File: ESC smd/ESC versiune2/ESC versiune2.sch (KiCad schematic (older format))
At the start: 92 parts, among them J1 Conn_01x03, J2 Conn_01x03, J3 Conn_01x03, J4 Conn_01x03, J5 Conn_01x02, J6 Conn_01x03, J7 Conn_01x02, Q3 IRLB8721PBF, Q4 IRLB8721PBF, Q5 IRLB8721PBF, Q6 IRLB8721PBF, Q7 IRLB8721PBF, Q8 IRLB8721PBF, U1 L7805, U2 ACS711xLCTR-12AB, U3 LP2950-3.3_TO92, U4 IR2101, U5 IR2101, U6 IR2101, U7 LM393, U8 LM393

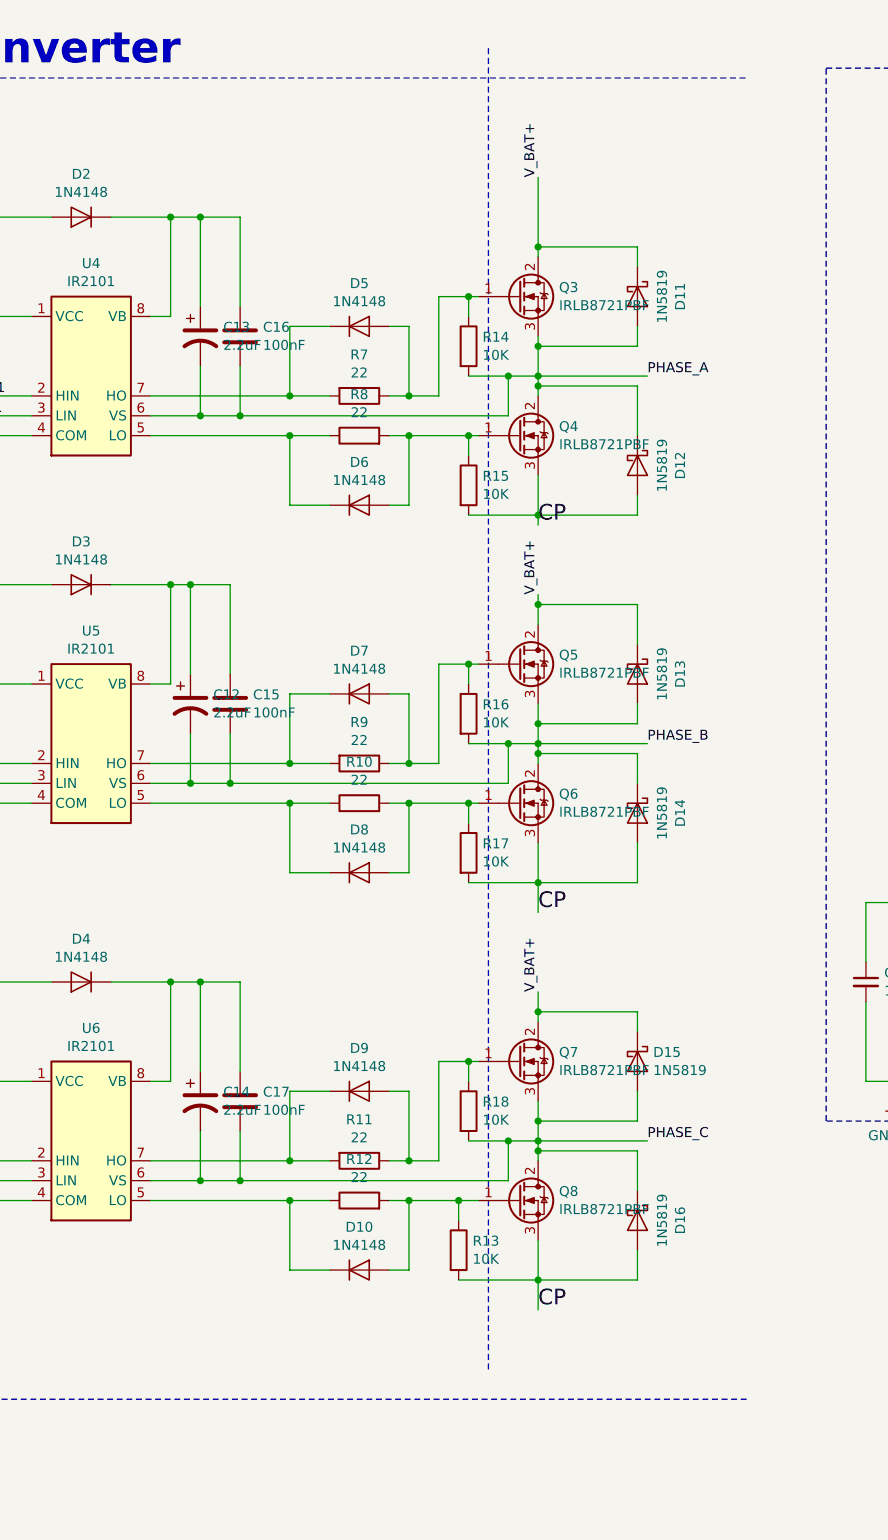
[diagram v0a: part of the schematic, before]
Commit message: SMD version
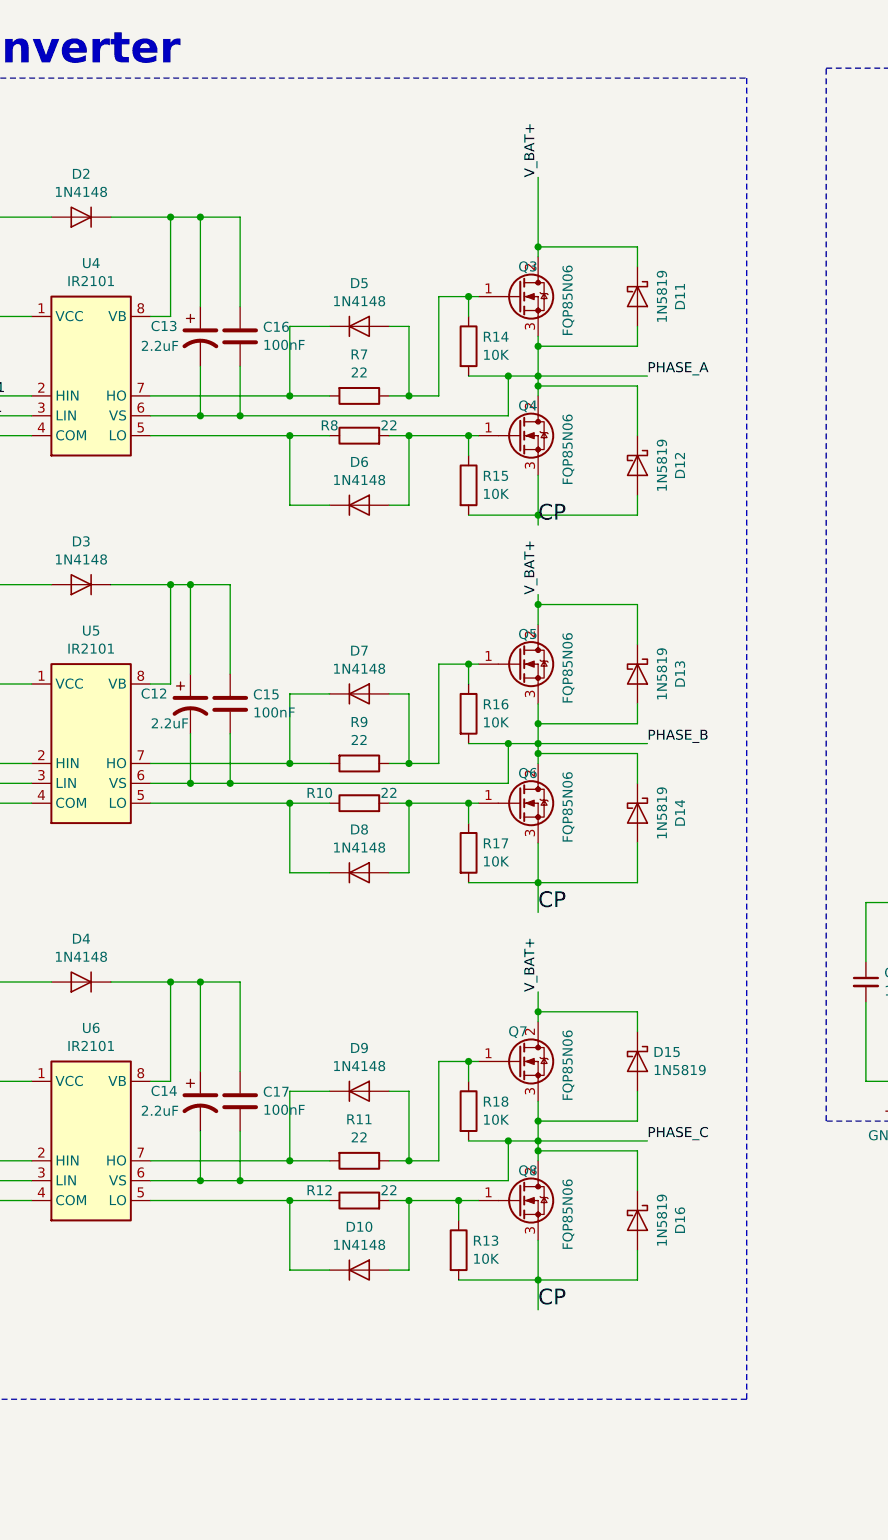
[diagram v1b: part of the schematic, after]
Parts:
- Q3, Q4, Q5, Q6, Q7, Q8: value IRLB8721PBF -> FQP85N06
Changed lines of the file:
@@
 Wire Wire Line
 	8000 4300 8200 4300
-Connection ~ 8000 4300
 Wire Wire Line
 	8000 4750 8000 4300
@@
 	10800 8400 5400 8400
 Wire Notes Line
-	9500 1600 9500 8250
+	10800 1750 10800 8400
 Wire Notes Line
 	5400 1750 10800 1750
@@
 AR Path="/5CB0A3AA" Ref="R12"  Part="1"
 AR Path="/5CB00088/5CB0A3AA" Ref="R?"  Part="1"
-F 0 "R12" V 9057 7400 50  0000 C CNN
-F 1 "22" V 8966 7400 50  0000 C CNN
+F 0 "R12" V 8900 7600 50  0000 C CNN
+F 1 "22" V 8900 7250 50  0000 C CNN
 F 2 "Resistor_SMD:R_2512_6332Metric_Pad1.52x3.35mm_HandSolder" V 8780 7400 50  0001 C CNN
 F 3 "~" H 8850 7400 50  0001 C CNN
@@
 	8200 4300 8200 4750
 Wire Wire Line
-	8000 5300 8200 5300
-Wire Wire Line
-	8200 5300 9600 5300
-Connection ~ 8200 5300
-Wire Wire Line
 	8200 5050 8200 5300
 $Comp
@@
 AR Path="/5CB0A348" Ref="R10"  Part="1"
 AR Path="/5CB00088/5CB0A348" Ref="R?"  Part="1"
-F 0 "R10" V 9057 5400 50  0000 C CNN
-F 1 "22" V 8966 5400 50  0000 C CNN
+F 0 "R10" V 8900 5600 50  0000 C CNN
+F 1 "22" V 8900 5250 50  0000 C CNN
 F 2 "Resistor_SMD:R_2512_6332Metric_Pad1.52x3.35mm_HandSolder" V 8780 5400 50  0001 C CNN
 F 3 "~" H 8850 5400 50  0001 C CNN
@@
 AR Path="/5CB0A2E7" Ref="R8"  Part="1"
 AR Path="/5CB00088/5CB0A2E7" Ref="R?"  Part="1"
-F 0 "R8" V 9057 3550 50  0000 C CNN
-F 1 "22" V 8966 3550 50  0000 C CNN
+F 0 "R8" V 8900 3700 50  0000 C CNN
+F 1 "22" V 8900 3400 50  0000 C CNN
 F 2 "Resistor_SMD:R_2512_6332Metric_Pad1.52x3.35mm_HandSolder" V 8780 3550 50  0001 C CNN
 F 3 "~" H 8850 3550 50  0001 C CNN
@@
 U 1 1 5CDD0D9C
 P 8050 3050
-F 0 "C13" H 8165 3096 50  0000 L CNN
-F 1 "2.2uF" H 8165 3005 50  0000 L CNN
+F 0 "C13" H 7800 3100 50  0000 L CNN
+F 1 "2.2uF" H 7750 3000 50  0000 L CNN
 F 2 "Capacitor_SMD:C_1206_3216Metric_Pad1.42x1.75mm_HandSolder" H 8050 3050 50  0001 C CNN
 F 3 "~" H 8050 3050 50  0001 C CNN
@@
 U 1 1 5CE448DD
 P 8000 4900
-F 0 "C12" H 8115 4946 50  0000 L CNN
-F 1 "2.2uF" H 8115 4855 50  0000 L CNN
+F 0 "C12" H 7750 4950 50  0000 L CNN
+F 1 "2.2uF" H 7800 4800 50  0000 L CNN
 F 2 "Capacitor_SMD:C_1206_3216Metric_Pad1.42x1.75mm_HandSolder" H 8000 4900 50  0001 C CNN
 F 3 "~" H 8000 4900 50  0001 C CNN
@@
 U 1 1 5CE923AF
 P 8050 6900
-F 0 "C14" H 8165 6946 50  0000 L CNN
-F 1 "2.2uF" H 8165 6855 50  0000 L CNN
+F 0 "C14" H 7800 6950 50  0000 L CNN
+F 1 "2.2uF" H 7750 6850 50  0000 L CNN
 F 2 "Capacitor_SMD:C_1206_3216Metric_Pad1.42x1.75mm_HandSolder" H 8050 6900 50  0001 C CNN
 F 3 "~" H 8050 6900 50  0001 C CNN
@@
 U 1 1 5CEC143D
 P 9650 2850
-F 0 "Q3" H 9855 2896 50  0000 L CNN
-F 1 "IRLB8721PBF" H 9855 2805 50  0000 L CNN
+F 0 "Q3" H 9650 3000 50  0000 L CNN
+F 1 "FQP85N06" V 9900 2650 50  0000 L CNN
 F 2 "Package_TO_SOT_SMD:TO-252-2" H 9900 2775 50  0001 L CIN
 F 3 "http://www.infineon.com/dgdl/irlb8721pbf.pdf?fileId=5546d462533600a40153566056732591" H 9650 2850 50  0001 L CNN
@@
 U 1 1 5CF35D4B
 P 9650 3550
-F 0 "Q4" H 9855 3596 50  0000 L CNN
-F 1 "IRLB8721PBF" H 9855 3505 50  0000 L CNN
+F 0 "Q4" H 9650 3700 50  0000 L CNN
+F 1 "FQP85N06" V 9900 3300 50  0000 L CNN
 F 2 "Package_TO_SOT_SMD:TO-252-2" H 9900 3475 50  0001 L CIN
 F 3 "http://www.infineon.com/dgdl/irlb8721pbf.pdf?fileId=5546d462533600a40153566056732591" H 9650 3550 50  0001 L CNN
@@
 U 1 1 5CF8368B
 P 9650 4700
-F 0 "Q5" H 9855 4746 50  0000 L CNN
-F 1 "IRLB8721PBF" H 9855 4655 50  0000 L CNN
+F 0 "Q5" H 9650 4850 50  0000 L CNN
+F 1 "FQP85N06" V 9900 4500 50  0000 L CNN
 F 2 "Package_TO_SOT_SMD:TO-252-2" H 9900 4625 50  0001 L CIN
 F 3 "http://www.infineon.com/dgdl/irlb8721pbf.pdf?fileId=5546d462533600a40153566056732591" H 9650 4700 50  0001 L CNN
@@
 U 1 1 5CFD0FCC
 P 9650 5400
-F 0 "Q6" H 9855 5446 50  0000 L CNN
-F 1 "IRLB8721PBF" H 9855 5355 50  0000 L CNN
+F 0 "Q6" H 9650 5550 50  0000 L CNN
+F 1 "FQP85N06" V 9900 5200 50  0000 L CNN
 F 2 "Package_TO_SOT_SMD:TO-252-2" H 9900 5325 50  0001 L CIN
 F 3 "http://www.infineon.com/dgdl/irlb8721pbf.pdf?fileId=5546d462533600a40153566056732591" H 9650 5400 50  0001 L CNN
@@
 U 1 1 5D01E912
 P 9650 6700
-F 0 "Q7" H 9855 6746 50  0000 L CNN
-F 1 "IRLB8721PBF" H 9855 6655 50  0000 L CNN
+F 0 "Q7" H 9600 6850 50  0000 L CNN
+F 1 "FQP85N06" V 9900 6500 50  0000 L CNN
 F 2 "Package_TO_SOT_SMD:TO-252-2" H 9900 6625 50  0001 L CIN
 F 3 "http://www.infineon.com/dgdl/irlb8721pbf.pdf?fileId=5546d462533600a40153566056732591" H 9650 6700 50  0001 L CNN
@@
 U 1 1 5D06C1F5
 P 9650 7400
-F 0 "Q8" H 9855 7446 50  0000 L CNN
-F 1 "IRLB8721PBF" H 9855 7355 50  0000 L CNN
+F 0 "Q8" H 9650 7550 50  0000 L CNN
+F 1 "FQP85N06" V 9900 7150 50  0000 L CNN
 F 2 "Package_TO_SOT_SMD:TO-252-2" H 9900 7325 50  0001 L CIN
 F 3 "http://www.infineon.com/dgdl/irlb8721pbf.pdf?fileId=5546d462533600a40153566056732591" H 9650 7400 50  0001 L CNN
@@
 Wire Wire Line
 	1400 9600 3200 9600
+Wire Wire Line
+	8000 5300 8200 5300
+Wire Wire Line
+	8200 5300 9600 5300
+Connection ~ 8200 5300
+Connection ~ 8000 4300
 $EndSCHEMATC
